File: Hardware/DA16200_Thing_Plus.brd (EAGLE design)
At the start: 22.9 x 58.4 mm, 103 parts, among them J2 THING_PLUS, J3 Qwiic, J5 USB C, J6 microSD, J7 CORTEX_JTAG_DEBUG_PTH_NS, Q1 20V/4.2A/52mΩ/1.4W, U1 DA16200MOD, U2 CH340E_MSOP10, U3 MCP73831, U5 4MB Flash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

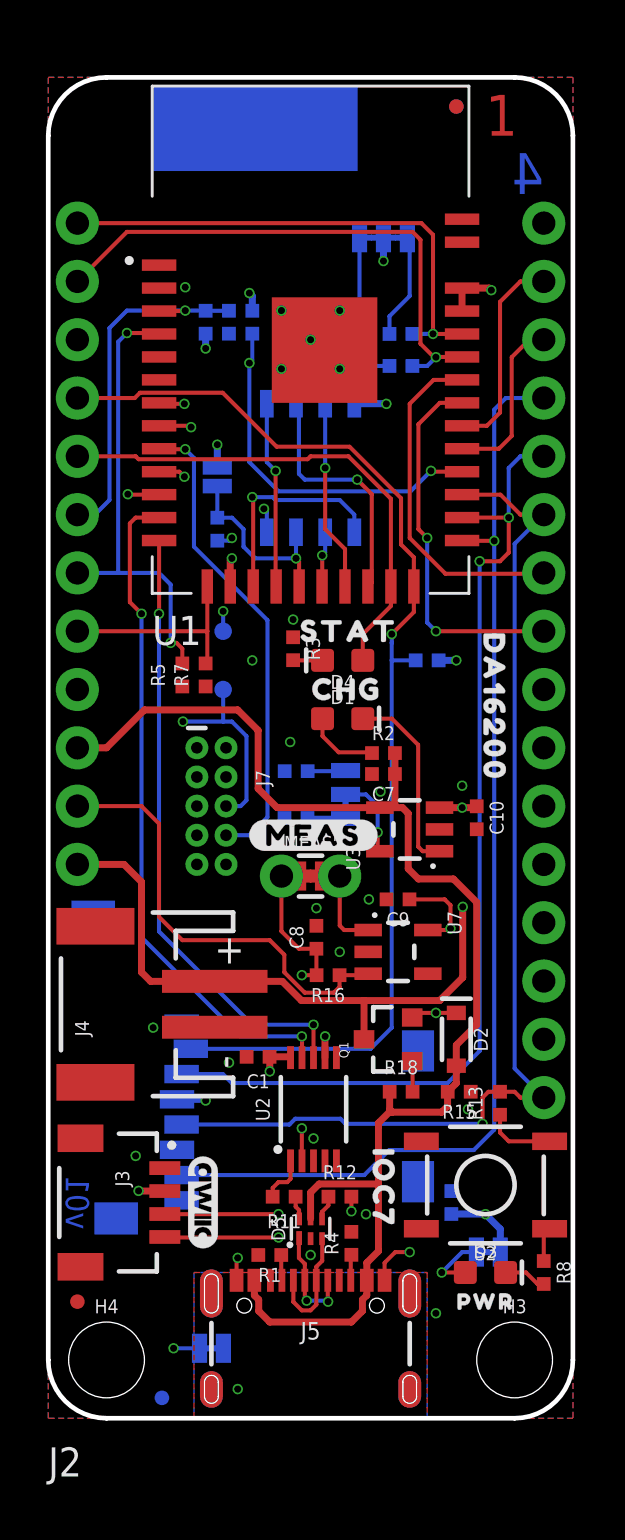
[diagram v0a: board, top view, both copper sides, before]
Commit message: Add GND vias to board
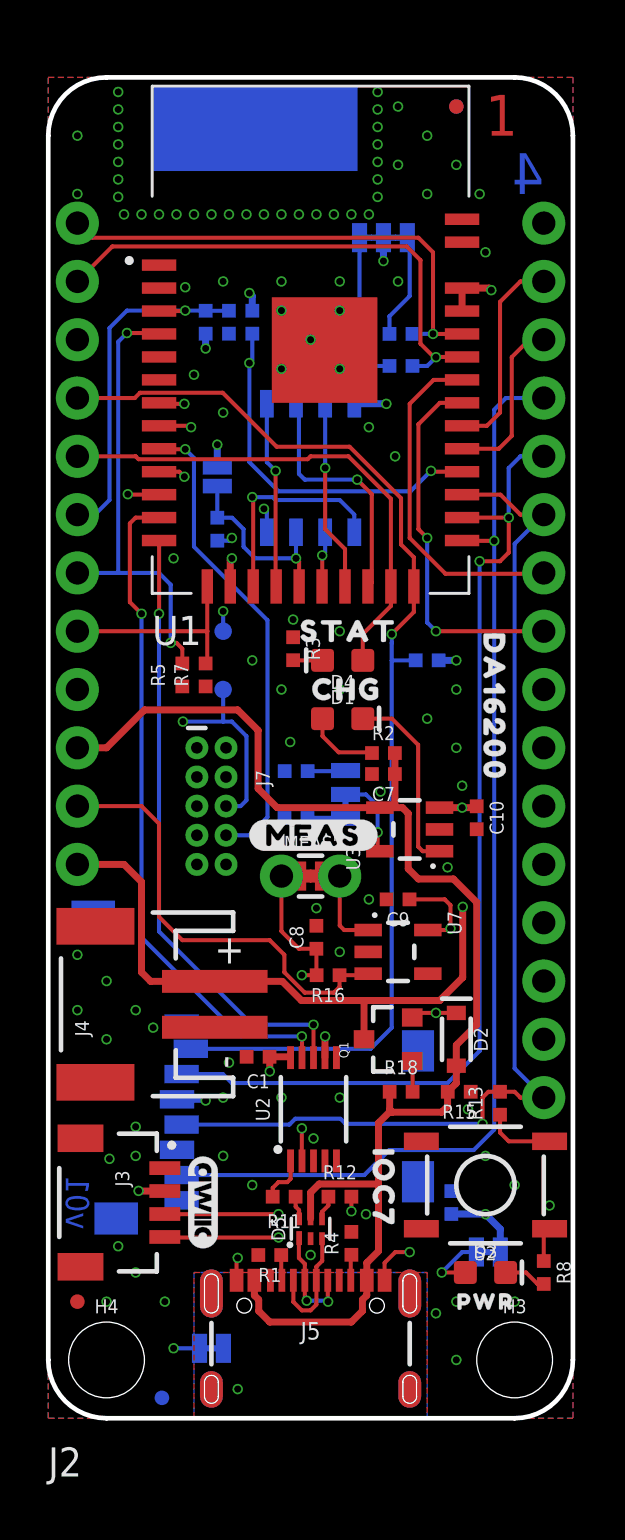
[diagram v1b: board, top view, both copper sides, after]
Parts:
- moved U$56 0.38 mm to (16.3, 34.3)
- moved U$80 0.25 mm to (15.5, 32.6)
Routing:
- net I2C_SCL: track 72.8 -> 71.8 mm
- net GND: vias 27 -> 102
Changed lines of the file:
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@@
 <?xml version="1.0" encoding="utf-8"?>
 <!DOCTYPE eagle SYSTEM "eagle.dtd">
-<eagle version="9.5.2">
+<eagle version="9.4.2">
 <drawing>
 <settings>
-<setting alwaysvectorfont="no"/>
+<setting alwaysvectorfont="yes"/>
 <setting keepoldvectorfont="yes"/>
 <setting verticaltext="up"/>
@@
 <layer number="95" name="Names" color="7" fill="1" visible="no" active="no"/>
 <layer number="96" name="Values" color="7" fill="1" visible="no" active="no"/>
-<layer number="2" name="gndvert" color="10" fill="7" visible="no" active="yes"/>
-<layer number="15" name="pwrhorz" color="4" fill="7" visible="no" active="yes"/>
+<layer number="2" name="gndvert" color="10" fill="7" visible="yes" active="yes"/>
+<layer number="15" name="pwrhorz" color="4" fill="7" visible="yes" active="yes"/>
 <layer number="3" name="Route3" color="4" fill="3" visible="no" active="no"/>
 <layer number="4" name="Route4" color="1" fill="4" visible="no" active="no"/>
@@
 <element name="U$79" library="output" package="#VBT#0" value="" x="6.096" y="24.13" smashed="yes" rot="MR0"/>
 <element name="U$52" library="output" package="#VUB#0" value="" x="6.096" y="29.21" smashed="yes" rot="MR0"/>
-<element name="U$56" library="output" package="THING_PLUS0" value="" x="15.875" y="34.29" smashed="yes" rot="MR0"/>
-<element name="U$80" library="output" package="DA162000" value="" x="15.24" y="32.639" smashed="yes" rot="MR0"/>
+<element name="U$56" library="output" package="THING_PLUS0" value="" x="16.256" y="34.29" smashed="yes" rot="MR0"/>
+<element name="U$80" library="output" package="DA162000" value="" x="15.494" y="32.639" smashed="yes" rot="MR0"/>
 <element name="U$81" library="output" package="DA162000" value="" x="19.431" y="34.925" smashed="yes" rot="R270"/>
 <element name="U$82" library="output" package="#I�C#0" value="" x="16.383" y="49.784" smashed="yes" rot="MR0"/>
@@
 <vertex x="0" y="58.42"/>
 </polygon>
+<via x="3.048" y="57.785" extent="1-16" drill="0.3048"/>
+<via x="3.048" y="57.023" extent="1-16" drill="0.3048"/>
+<via x="3.048" y="56.261" extent="1-16" drill="0.3048"/>
+<via x="3.048" y="55.499" extent="1-16" drill="0.3048"/>
+<via x="3.048" y="54.737" extent="1-16" drill="0.3048"/>
+<via x="3.048" y="53.975" extent="1-16" drill="0.3048"/>
+<via x="3.048" y="53.213" extent="1-16" drill="0.3048"/>
+<via x="3.302" y="52.451" extent="1-16" drill="0.3048"/>
+<via x="4.064" y="52.451" extent="1-16" drill="0.3048"/>
+<via x="4.826" y="52.451" extent="1-16" drill="0.3048"/>
+<via x="5.588" y="52.451" extent="1-16" drill="0.3048"/>
+<via x="6.35" y="52.451" extent="1-16" drill="0.3048"/>
+<via x="7.112" y="52.451" extent="1-16" drill="0.3048"/>
+<via x="7.874" y="52.451" extent="1-16" drill="0.3048"/>
+<via x="8.636" y="52.451" extent="1-16" drill="0.3048"/>
+<via x="9.398" y="52.451" extent="1-16" drill="0.3048"/>
+<via x="10.16" y="52.451" extent="1-16" drill="0.3048"/>
+<via x="10.922" y="52.451" extent="1-16" drill="0.3048"/>
+<via x="11.684" y="52.451" extent="1-16" drill="0.3048"/>
+<via x="12.446" y="52.451" extent="1-16" drill="0.3048"/>
+<via x="13.208" y="52.451" extent="1-16" drill="0.3048"/>
+<via x="13.97" y="52.451" extent="1-16" drill="0.3048"/>
+<via x="14.351" y="53.213" extent="1-16" drill="0.3048"/>
+<via x="14.351" y="53.975" extent="1-16" drill="0.3048"/>
+<via x="14.351" y="54.737" extent="1-16" drill="0.3048"/>
+<via x="14.351" y="55.499" extent="1-16" drill="0.3048"/>
+<via x="14.351" y="56.261" extent="1-16" drill="0.3048"/>
+<via x="14.351" y="57.023" extent="1-16" drill="0.3048"/>
+<via x="14.351" y="57.785" extent="1-16" drill="0.3048"/>
+<via x="1.27" y="55.88" extent="1-16" drill="0.3048"/>
+<via x="1.27" y="53.34" extent="1-16" drill="0.3048"/>
+<via x="15.24" y="57.15" extent="1-16" drill="0.3048"/>
+<via x="16.51" y="55.88" extent="1-16" drill="0.3048"/>
+<via x="15.24" y="54.61" extent="1-16" drill="0.3048"/>
+<via x="17.78" y="54.61" extent="1-16" drill="0.3048"/>
+<via x="16.51" y="53.34" extent="1-16" drill="0.3048"/>
+<via x="18.796" y="53.34" extent="1-16" drill="0.3048"/>
+<via x="19.05" y="50.8" extent="1-16" drill="0.3048"/>
+<via x="15.24" y="49.53" extent="1-16" drill="0.3048"/>
+<via x="12.7" y="49.53" extent="1-16" drill="0.3048"/>
+<via x="10.16" y="49.53" extent="1-16" drill="0.3048"/>
+<via x="7.62" y="49.53" extent="1-16" drill="0.3048"/>
+<via x="6.35" y="45.466" extent="1-16" drill="0.3048"/>
+<via x="7.62" y="43.815" extent="1-16" drill="0.3048"/>
+<via x="13.97" y="43.18" extent="1-16" drill="0.3048"/>
+<via x="15.113" y="41.91" extent="1-16" drill="0.3048"/>
+<via x="5.461" y="37.465" extent="1-16" drill="0.3048"/>
+<via x="10.16" y="31.75" extent="1-16" drill="0.3048"/>
+<via x="12.7" y="34.29" extent="1-16" drill="0.3048"/>
+<via x="17.78" y="31.75" extent="1-16" drill="0.3048"/>
+<via x="16.51" y="30.48" extent="1-16" drill="0.3048"/>
+<via x="17.78" y="29.21" extent="1-16" drill="0.3048"/>
+<via x="17.399" y="24.003" extent="1-16" drill="0.3048"/>
+<via x="1.27" y="20.193" extent="1-16" drill="0.3048"/>
+<via x="2.54" y="19.05" extent="1-16" drill="0.3048"/>
+<via x="3.81" y="17.78" extent="1-16" drill="0.3048"/>
+<via x="1.27" y="17.78" extent="1-16" drill="0.3048"/>
+<via x="2.54" y="16.51" extent="1-16" drill="0.3048"/>
+<via x="3.81" y="12.7" extent="1-16" drill="0.3048"/>
+<via x="2.667" y="11.303" extent="1-16" drill="0.3048"/>
+<via x="3.048" y="7.493" extent="1-16" drill="0.3048"/>
+<via x="3.81" y="6.35" extent="1-16" drill="0.3048"/>
+<via x="2.54" y="5.08" extent="1-16" drill="0.3048"/>
+<via x="5.08" y="5.08" extent="1-16" drill="0.3048"/>
+<via x="17.78" y="2.54" extent="1-16" drill="0.3048"/>
+<via x="17.78" y="5.08" extent="1-16" drill="0.3048"/>
+<via x="20.32" y="5.08" extent="1-16" drill="0.3048"/>
+<via x="21.844" y="9.271" extent="1-16" drill="0.3048"/>
+<via x="20.32" y="10.16" extent="1-16" drill="0.3048"/>
+<via x="19.05" y="11.43" extent="1-16" drill="0.3048"/>
+<via x="8.89" y="10.16" extent="1-16" drill="0.3048"/>
+<via x="7.62" y="11.43" extent="1-16" drill="0.3048"/>
+<via x="12.7" y="13.97" extent="1-16" drill="0.3048"/>
+<via x="10.16" y="13.97" extent="1-16" drill="0.3048"/>
+<via x="7.62" y="13.97" extent="1-16" drill="0.3048"/>
 </signal>
 <signal name="V_USB">
@@
 <via x="16.764" y="47.244" extent="1-16" drill="0.3048"/>
 <wire x1="16.764" y1="47.244" x2="15.867" y2="47.244" width="0.1778" layer="16"/>
-<wire x1="1.27" y1="52.07" x2="16.256" y2="52.07" width="0.1778" layer="1"/>
-<wire x1="16.256" y1="52.07" x2="16.764" y2="51.562" width="0.1778" layer="1"/>
-<wire x1="16.764" y1="51.562" x2="16.764" y2="47.244" width="0.1778" layer="1"/>
+<wire x1="16.129" y1="51.435" x2="1.905" y2="51.435" width="0.1778" layer="1"/>
+<wire x1="1.27" y1="52.07" x2="1.905" y2="51.435" width="0.1778" layer="1"/>
+<wire x1="16.129" y1="51.435" x2="16.764" y2="50.8" width="0.1778" layer="1"/>
+<wire x1="16.764" y1="50.8" x2="16.764" y2="47.244" width="0.1778" layer="1"/>
 <wire x1="16.764" y1="47.244" x2="16.256" y2="47.244" width="0.1778" layer="2"/>
 <wire x1="16.256" y1="47.244" x2="15.621" y2="46.609" width="0.1778" layer="2"/>
@@
 <wire x1="16.891" y1="46.228" x2="16.51" y2="45.847" width="0.1778" layer="16"/>
 <wire x1="16.51" y1="45.847" x2="15.867" y2="45.847" width="0.1778" layer="16"/>
-<wire x1="1.27" y1="49.53" x2="3.429" y2="51.689" width="0.1778" layer="1"/>
+<wire x1="1.27" y1="49.53" x2="2.794" y2="51.054" width="0.1778" layer="1"/>
 <wire x1="16.891" y1="46.228" x2="16.8063" y2="46.228" width="0.1778" layer="1"/>
 <wire x1="16.8063" y1="46.228" x2="16.2179" y2="46.8164" width="0.1778" layer="1"/>
-<wire x1="16.2179" y1="51.3461" x2="16.2179" y2="46.8164" width="0.1778" layer="1"/>
-<wire x1="3.429" y1="51.689" x2="15.875" y2="51.689" width="0.1778" layer="1"/>
-<wire x1="15.875" y1="51.689" x2="16.2179" y2="51.3461" width="0.1778" layer="1"/>
+<wire x1="16.2179" y1="50.4571" x2="16.2179" y2="46.8164" width="0.1778" layer="1"/>
+<wire x1="2.794" y1="51.054" x2="15.621" y2="51.054" width="0.1778" layer="1"/>
+<wire x1="15.621" y1="51.054" x2="16.2179" y2="50.4571" width="0.1778" layer="1"/>
 <wire x1="16.891" y1="46.228" x2="16.002" y2="45.339" width="0.1778" layer="2"/>
 <wire x1="16.002" y1="45.339" x2="16.002" y2="8.89" width="0.1778" layer="2"/>
@@
 <wire x1="11.938" y1="23.622" x2="12.7" y2="23.622" width="0.1778" layer="1"/>
 </signal>
+<signal name="N$27">
+<via x="12.7" y="31.75" extent="1-16" drill="0.3048"/>
+</signal>
 </signals>

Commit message: Updated a few parts
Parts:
- R19: value 10K -> 10k; device SparkFun-Resistors:0402-TIGHT -> SparkFun-Resistors:0402

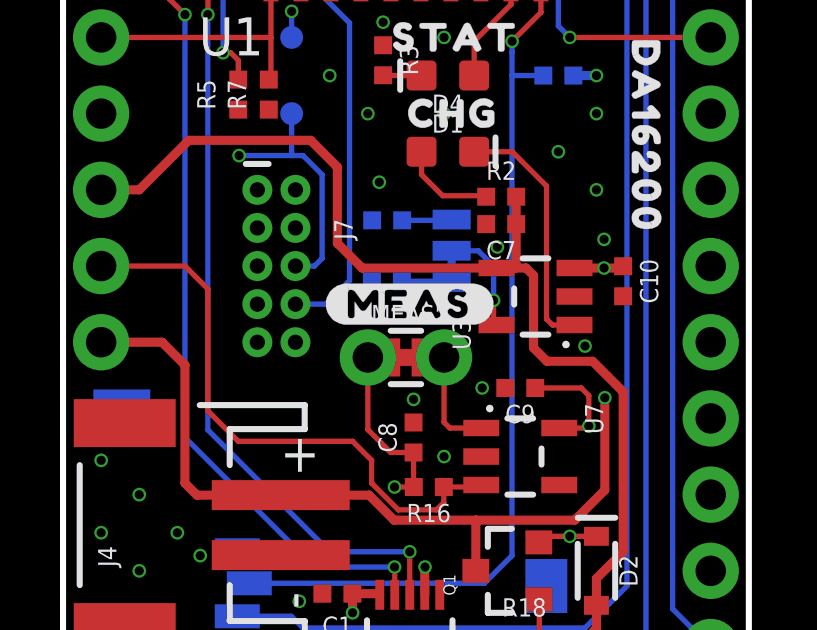
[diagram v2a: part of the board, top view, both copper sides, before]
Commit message: Fix some names on schematic
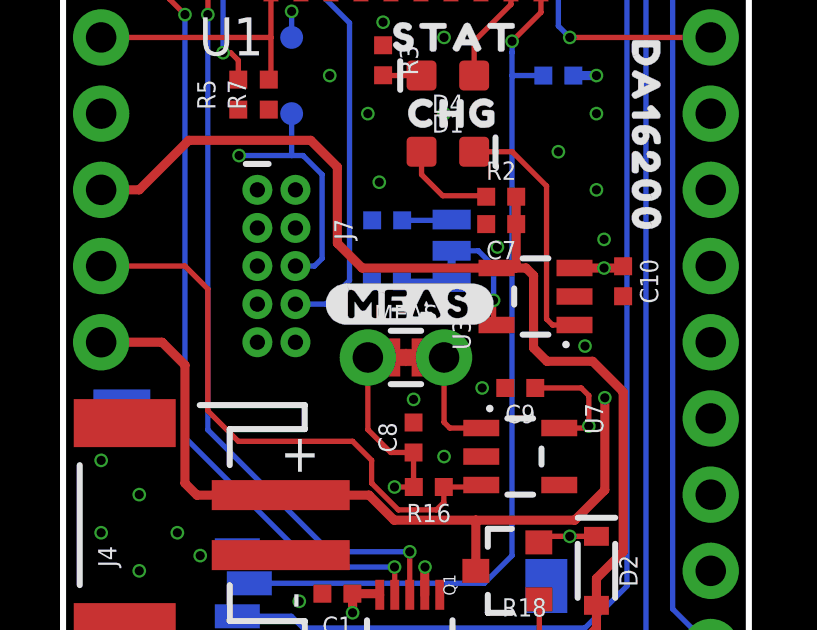
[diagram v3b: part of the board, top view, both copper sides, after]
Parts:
- renumbered MEAS' to MEAS
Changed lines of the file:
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@@
 <?xml version="1.0" encoding="utf-8"?>
 <!DOCTYPE eagle SYSTEM "eagle.dtd">
-<eagle version="9.5.2">
+<eagle version="9.4.2">
 <drawing>
 <settings>
-<setting alwaysvectorfont="no"/>
+<setting alwaysvectorfont="yes"/>
 <setting keepoldvectorfont="yes"/>
 <setting verticaltext="up"/>
@@
 <attribute name="VALUE" x="6.223" y="41.021" size="0.6096" layer="28" font="vector" ratio="20" rot="MR90" align="top-center"/>
 </element>
-<element name="MEAS'" library="SparkFun-Jumpers" package="COMBO-JUMPER_2_NC_TRACE" value="JUMPER-COMBO_2_NC_TRACE" x="11.43" y="23.622" smashed="yes">
+<element name="MEAS" library="SparkFun-Jumpers" package="COMBO-JUMPER_2_NC_TRACE" value="JUMPER-COMBO_2_NC_TRACE" x="11.43" y="23.622" smashed="yes">
 <attribute name="NAME" x="11.43" y="24.765" size="0.6096" layer="25" font="vector" ratio="20" align="bottom-center"/>
 <attribute name="VALUE" x="11.43" y="22.479" size="0.6096" layer="27" font="vector" ratio="20" align="top-center"/>
@@
 <contactref element="R16" pad="2"/>
 <contactref element="C8" pad="1"/>
-<contactref element="MEAS'" pad="3"/>
-<contactref element="MEAS'" pad="1"/>
+<contactref element="MEAS" pad="3"/>
+<contactref element="MEAS" pad="1"/>
 <wire x1="11.692" y1="19.304" x2="11.684" y2="19.312" width="0.1778" layer="1"/>
 <wire x1="11.684" y1="19.312" x2="11.684" y2="20.455" width="0.1778" layer="1"/>
@@
 </signal>
 <signal name="N$22">
-<contactref element="MEAS'" pad="2"/>
-<contactref element="MEAS'" pad="4"/>
+<contactref element="MEAS" pad="2"/>
+<contactref element="MEAS" pad="4"/>
 <contactref element="U7" pad="1"/>
 <wire x1="13.9399" y1="21.27" x2="12.893" y2="21.27" width="0.1778" layer="1"/>

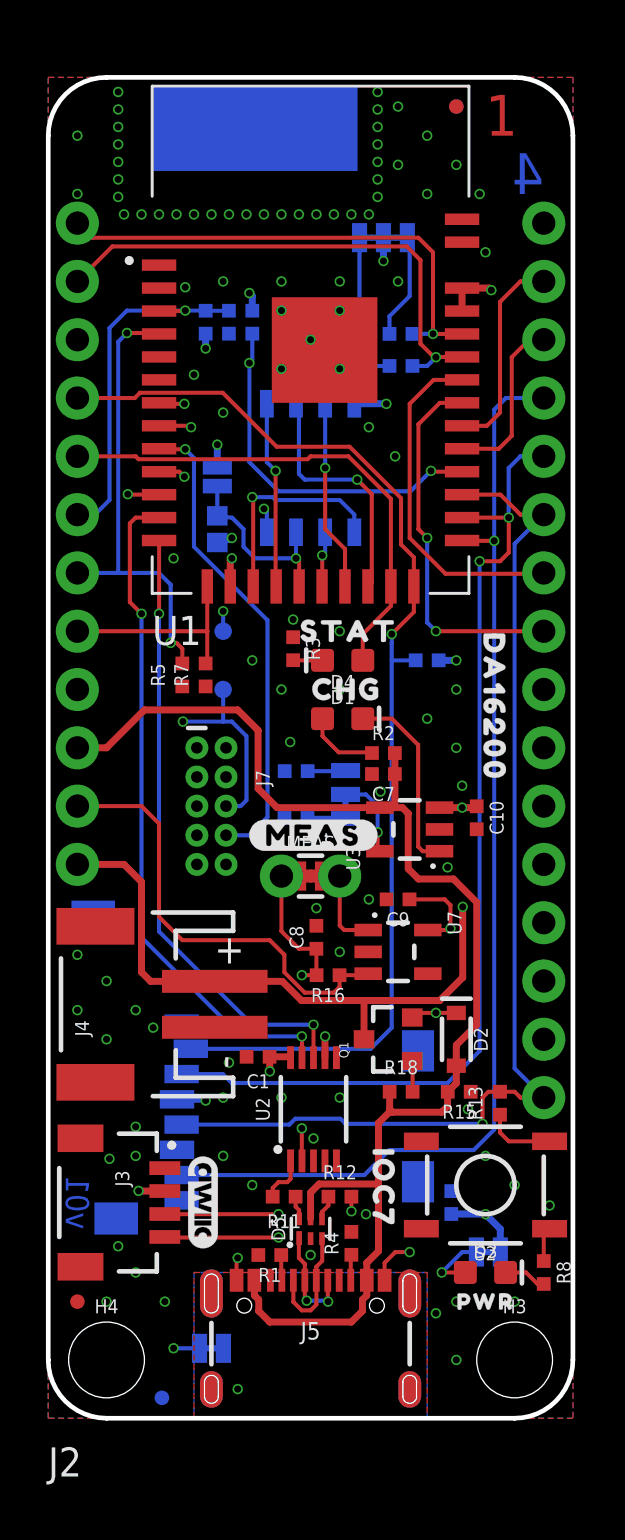
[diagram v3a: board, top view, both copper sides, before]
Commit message: Move LiPo, JTAG connector, and MEAS jumper to make room for connectors.
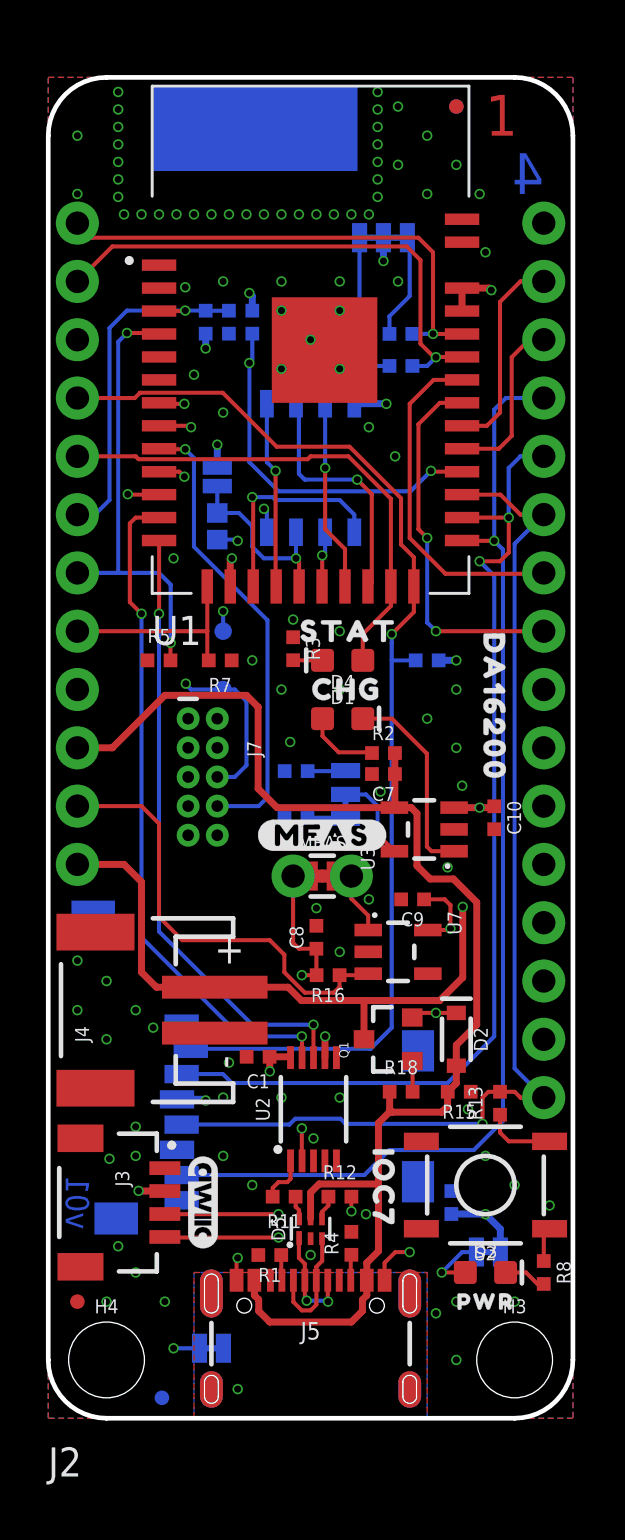
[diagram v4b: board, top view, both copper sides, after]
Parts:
- moved J7 1.33 mm to (6.73, 27.9)
- moved R5 1.20 mm to (4.83, 33.0), turned to 0 degrees
- moved R7 0.90 mm to (7.49, 33.0), turned to 180 degrees
- moved C10 0.76 mm to (19.4, 26.2)
- moved C9 0.63 mm to (15.9, 22.6)
- moved U3 0.63 mm to (16.4, 25.7)
- moved MEAS 0.51 mm to (11.9, 23.6)
- moved U$8 0.38 mm to (9.14, 25.4)
- moved U$3 0.38 mm to (18.9, 23.6)
- moved J4 0.25 mm to (3.56, 17.8)
- moved R19 0.13 mm to (7.37, 38.9)
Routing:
- net GPIOC7: track 20.1 -> 17.5 mm
- net TCLK: track 17.3 -> 15.9 mm
- net TMS: track 18.5 -> 17.1 mm
- net GPIOC6: track 24.7 -> 25.8 mm
- net N$22: track 4.24 -> 3.42 mm
- net GPIOC8: track 20.8 -> 20.1 mm
- net 3.3V: track 21.5 -> 20.9 mm
- net SPI_PICO: track 43.9 -> 44.5 mm
